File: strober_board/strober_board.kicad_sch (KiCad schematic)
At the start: 25 parts, among them J1 Conn_01x02, J2 Conn_01x02, J3 Conn_01x02, J4 AVR-ISP-6, Q1 BC237, Q2 BC237, Q3 BS170, SW1 SW_Push, U1 L78L05_TO92, U2 EL817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

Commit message: changed connectors
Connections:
- net at D3.2 (A), D4.1 (K): now also J3.1 (Pin_1); no longer J1.2 (Pin_2)
- net at D1.2 (A), D2.1 (K): now also J3.2 (Pin_2); no longer J1.1 (Pin_1)
- net at D6.1 (K), R5.2: now also J1.2 (Pin_2); no longer J3.1 (Pin_1)
- net at D6.2 (A), Q3.1 (D): now also J1.1 (Pin_1); no longer J3.2 (Pin_2)
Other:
- moved on the sheet: J1, J3
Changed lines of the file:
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@@
 	(symbol
 		(lib_id "Connector_Generic:Conn_01x02")
-		(at 97.79 82.55 0)
+		(at 30.48 59.69 180)
 		(unit 1)
 		(exclude_from_sim no)
@@
 		(dnp no)
 		(property "Reference" "J3"
-			(at 97.79 87.63 0)
+			(at 30.48 54.61 0)
 			(effects
 				(font
@@
 		)
 		(property "Value" "Conn_01x02"
-			(at 97.79 88.9 0)
+			(at 30.48 53.34 0)
 			(effects
 				(font
@@
 		)
 		(property "Footprint" "Connector_Molex:Molex_KK-254_AE-6410-02A_1x02_P2.54mm_Vertical"
-			(at 97.79 82.55 0)
+			(at 30.48 59.69 0)
 			(effects
 				(font
@@
 		)
 		(property "Datasheet" "~"
-			(at 97.79 82.55 0)
+			(at 30.48 59.69 0)
 			(effects
 				(font
@@
 		)
 		(property "Description" "Generic connector, single row, 01x02, script generated (kicad-library-utils/schlib/autogen/connector/)"
-			(at 97.79 82.55 0)
+			(at 30.48 59.69 0)
 			(effects
 				(font
@@
 	(symbol
 		(lib_id "Connector_Generic:Conn_01x02")
-		(at 30.48 57.15 0)
-		(mirror y)
+		(at 97.79 85.09 0)
+		(mirror x)
 		(unit 1)
 		(exclude_from_sim no)
@@
 		(dnp no)
 		(property "Reference" "J1"
-			(at 30.226 62.484 0)
+			(at 98.044 79.756 0)
 			(effects
 				(font
@@
 		)
 		(property "Value" "Conn_01x02"
-			(at 30.48 63.5 0)
+			(at 97.79 78.74 0)
 			(effects
 				(font
@@
 		)
 		(property "Footprint" "Connector_JST:JST_EH_B2B-EH-A_1x02_P2.50mm_Vertical"
-			(at 30.48 57.15 0)
+			(at 97.79 85.09 0)
 			(effects
 				(font
@@
 		)
 		(property "Datasheet" "~"
-			(at 30.48 57.15 0)
+			(at 97.79 85.09 0)
 			(effects
 				(font
@@
 		)
 		(property "Description" "Generic connector, single row, 01x02, script generated (kicad-library-utils/schlib/autogen/connector/)"
-			(at 30.48 57.15 0)
-			(effects
-				(font
+			(at 97.79 85.09 0)
+			(effects
+				(font

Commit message: firmware readme
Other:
- note added: "Fixme! Reverse polarity protection is flawed! Doesn't cover load path!"
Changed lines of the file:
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@@
+		)
+	)
+	(text "Fixme! Reverse polarity protection is flawed!\nDoesn't cover load path!"
+		(exclude_from_sim no)
+		(at 12.7 24.384 0)
+		(effects
+			(font
+				(size 1.27 1.27)
+				(thickness 0.254)
+				(bold yes)
+			)
+			(justify left)
 		)
 	)

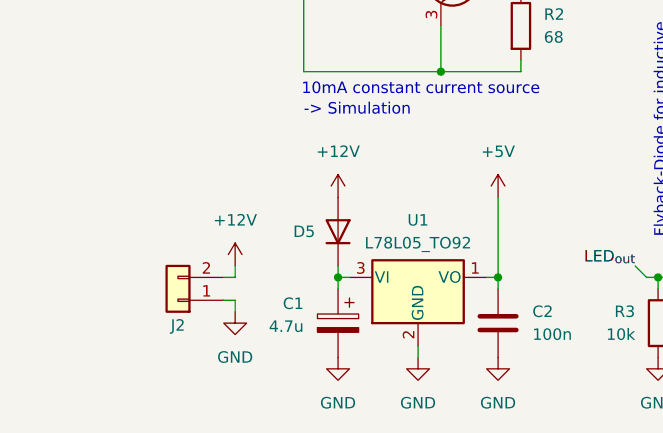
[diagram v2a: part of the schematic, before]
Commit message: Fixed reverse polarity protection
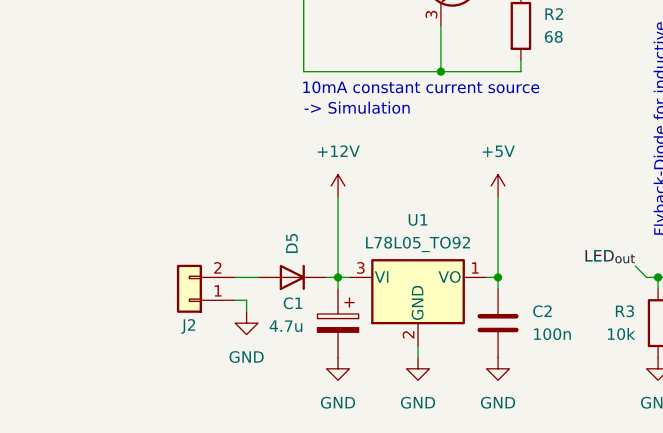
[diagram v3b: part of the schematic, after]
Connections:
- net +12V: now also C1.1, D5.1 (K), U1.3 (VI); no longer D5.2 (A), J2.2 (Pin_2)
- new net: D5.2 (A), J2.2 (Pin_2)
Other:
- moved on the sheet: D5, J2
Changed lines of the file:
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@@
 	(wire
 		(pts
-			(xy 35.56 95.25) (xy 36.83 95.25)
+			(xy 36.83 95.25) (xy 39.37 95.25)
 		)
 		(stroke
@@
 	(wire
 		(pts
-			(xy 36.83 97.79) (xy 35.56 97.79)
+			(xy 38.1 97.79) (xy 36.83 97.79)
 		)
 		(stroke
@@
 	(wire
 		(pts
-			(xy 36.83 99.06) (xy 36.83 97.79)
+			(xy 38.1 99.06) (xy 38.1 97.79)
 		)
 		(stroke
@@
 	(wire
 		(pts
-			(xy 48.26 93.98) (xy 48.26 95.25)
+			(xy 48.26 86.36) (xy 48.26 95.25)
 		)
 		(stroke
@@
 	(wire
 		(pts
-			(xy 36.83 95.25) (xy 36.83 93.98)
+			(xy 140.97 59.69) (xy 143.51 59.69)
 		)
 		(stroke
@@
 	(wire
 		(pts
-			(xy 140.97 59.69) (xy 143.51 59.69)
+			(xy 46.99 95.25) (xy 48.26 95.25)
 		)
 		(stroke
@@
 	(symbol
 		(lib_id "Device:D")
-		(at 48.26 90.17 270)
-		(mirror x)
+		(at 43.18 95.25 180)
 		(unit 1)
 		(exclude_from_sim no)
@@
 		(dnp no)
 		(property "Reference" "D5"
-			(at 45.72 90.17 90)
+			(at 43.18 92.71 90)
 			(effects
 				(font
@@
 		)
 		(property "Value" "D"
-			(at 45.72 91.4399 90)
+			(at 44.4499 92.71 90)
 			(effects
 				(font
@@
 		)
 		(property "Footprint" "Diode_THT:D_DO-15_P10.16mm_Horizontal"
-			(at 48.26 90.17 0)
+			(at 43.18 95.25 0)
 			(effects
 				(font
@@
 		)
 		(property "Datasheet" "~"
-			(at 48.26 90.17 0)
+			(at 43.18 95.25 0)
 			(effects
 				(font
@@
 		)
 		(property "Description" "Diode"
-			(at 48.26 90.17 0)
+			(at 43.18 95.25 0)
 			(effects
 				(font
@@
 		)
 		(property "Sim.Device" "D"
-			(at 48.26 90.17 0)
+			(at 43.18 95.25 0)
 			(effects
 				(font
@@
 		)
 		(property "Sim.Pins" "1=K 2=A"
-			(at 48.26 90.17 0)
+			(at 43.18 95.25 0)
 			(effects
 				(font
@@
 	(symbol
 		(lib_id "power:GND")
-		(at 36.83 99.06 0)
+		(at 38.1 99.06 0)
 		(unit 1)
 		(exclude_from_sim no)
@@
 		(fields_autoplaced yes)
 		(property "Reference" "#PWR02"
-			(at 36.83 105.41 0)
+			(at 38.1 105.41 0)
 			(effects
 				(font
@@
 		)
 		(property "Value" "GND"
-			(at 36.83 104.14 0)
+			(at 38.1 104.14 0)
 			(effects
 				(font
@@
 		)
 		(property "Footprint" ""
-			(at 36.83 99.06 0)
+			(at 38.1 99.06 0)
 			(effects
 				(font
@@
 		)
 		(property "Datasheet" ""
-			(at 36.83 99.06 0)
+			(at 38.1 99.06 0)
 			(effects
 				(font
@@
 		)
 		(property "Description" "Power symbol creates a global label with name \"GND\" , ground"
-			(at 36.83 99.06 0)
+			(at 38.1 99.06 0)
 			(effects
 				(font
@@
 	(symbol
 		(lib_id "Connector_Generic:Conn_01x02")
-		(at 30.48 97.79 180)
+		(at 31.75 97.79 180)
 		(unit 1)
 		(exclude_from_sim no)
@@
 		(dnp no)
 		(property "Reference" "J2"
-			(at 30.48 100.584 0)
+			(at 31.75 100.584 0)
 			(effects
 				(font
@@
 		)
 		(property "Value" "Conn_01x02"
-			(at 30.48 91.44 0)
+			(at 31.75 91.44 0)
 			(effects
 				(font
@@
 		)
 		(property "Footprint" "Connector_Molex:Molex_KK-254_AE-6410-02A_1x02_P2.54mm_Vertical"
-			(at 30.48 97.79 0)
+			(at 31.75 97.79 0)
 			(effects
 				(font
@@
 		)
 		(property "Datasheet" "~"
-			(at 30.48 97.79 0)
+			(at 31.75 97.79 0)
 			(effects
 				(font
@@
 		)
 		(property "Description" "Generic connector, single row, 01x02, script generated (kicad-library-utils/schlib/autogen/connector/)"
-			(at 30.48 97.79 0)
+			(at 31.75 97.79 0)
 			(effects
 				(font
@@
 					(unit 1)
 				)
-			)
-		)
-	)
-	(symbol
-		(lib_id "power:+12V")
-		(at 36.83 93.98 0)
-		(unit 1)
-		(exclude_from_sim no)
-		(in_bom yes)
-		(on_board yes)
-		(dnp no)
-		(fields_autoplaced yes)
-		(property "Reference" "#PWR01"
-			(at 36.83 97.79 0)
-			(effects
-				(font
-					(size 1.27 1.27)
-				)
-				(hide yes)
-			)
-		)
-		(property "Value" "+12V"
-			(at 36.83 88.9 0)
-			(effects
-				(font
-					(size 1.27 1.27)
-				)
-			)
-		)
-		(property "Footprint" ""
-			(at 36.83 93.98 0)
-			(effects
-				(font
-					(size 1.27 1.27)
-				)
-				(hide yes)
-			)
-		)
-		(property "Datasheet" ""
-			(at 36.83 93.98 0)
-			(effects
-				(font
-					(size 1.27 1.27)
-				)
-				(hide yes)
-			)
-		)
-		(property "Description" "Power symbol creates a global label with name \"+12V\""
-			(at 36.83 93.98 0)
-			(effects
-				(font
-					(size 1.27 1.27)
-				)
-				(hide yes)
-			)
-		)
-		(pin "1"
-		)
-		(instances
-			(project "whip_mod_board"
-				(path "/40cf83b7-ec3b-45bf-97f4-aa0389807d4b"
-					(reference "#PWR01")
-					(unit 1)
-				)

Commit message: minor board update
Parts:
- added C4: 100n, Resistor_THT:R_Axial_DIN0207_L6.3mm_D2.5mm_P10.16mm_Horizontal, symbol Device:C
- added J5: AVR-ISP-6, Connector_IDC:IDC-Header_2x03_P2.54mm_Vertical, symbol Connector:AVR-ISP-6
- added R6: 10k, Resistor_THT:R_Axial_DIN0207_L6.3mm_D2.5mm_P10.16mm_Horizontal, symbol Device:R
- added U4: ATtiny85-20P, Package_DIP:DIP-8_W7.62mm, symbol MCU_Microchip_ATtiny:ATtiny85-20P
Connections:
- net +5V: now also C4.1, J5.2 (VCC), R6.1, U4.8 (VCC)
- net GND: now also C4.2, J5.6 (GND), U4.4 (GND)
- net LED_{out}: now also U4.3 (XTAL2/PB4)
- net MISO: now also J5.1 (MISO), U4.6 (PB1)
- net MOSI: now also J5.4 (MOSI), U4.5 (AREF/PB0)
- net SCK: now also J5.3 (SCK), U4.7 (PB2)
- net Trigg_{in}: now also U4.2 (XTAL1/PB3)
- net ~{RST}: now also J5.5 (~{RST}), R6.2, U4.1 (~{RESET}/PB5)

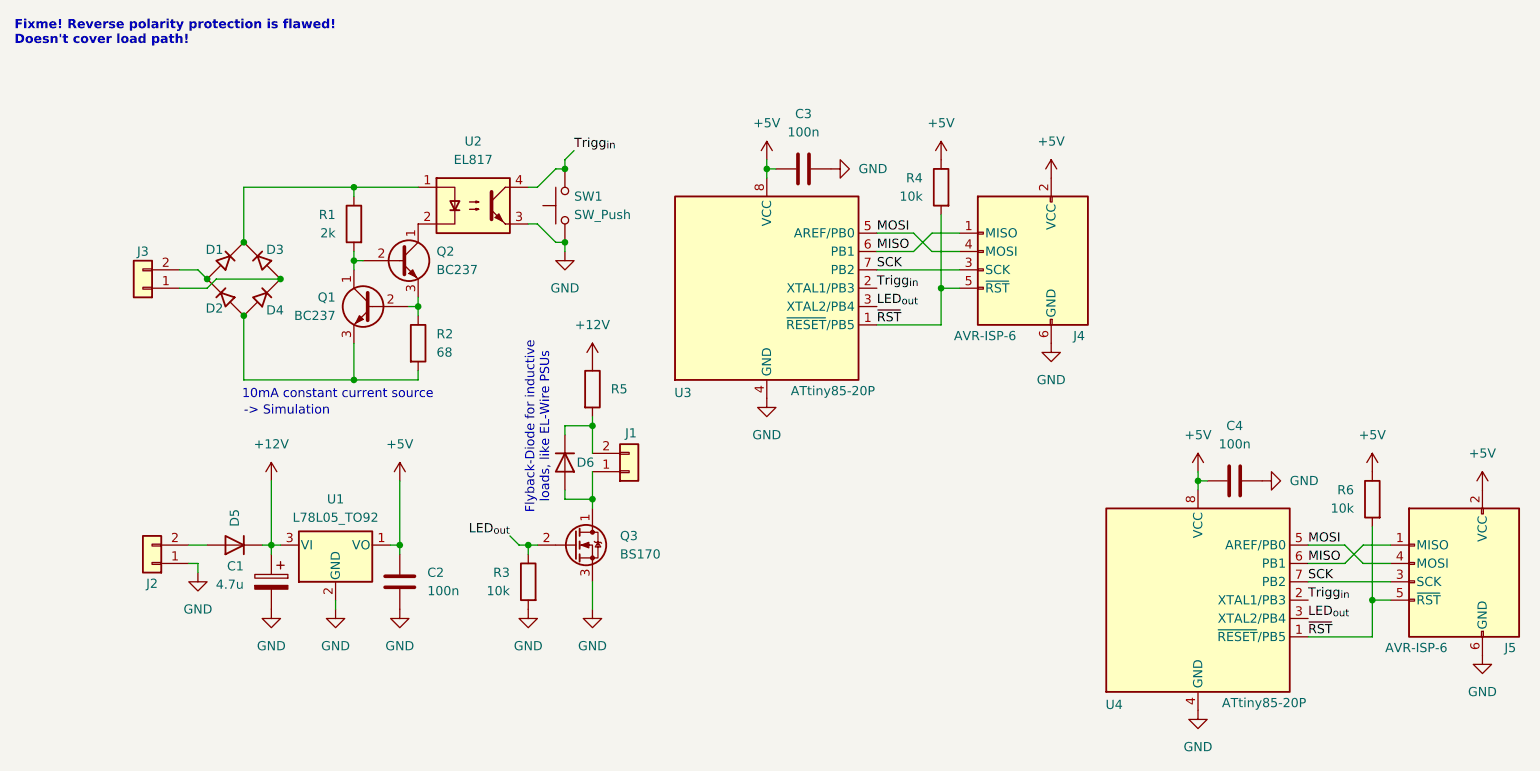
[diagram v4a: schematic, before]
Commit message: fix silkscreen typo
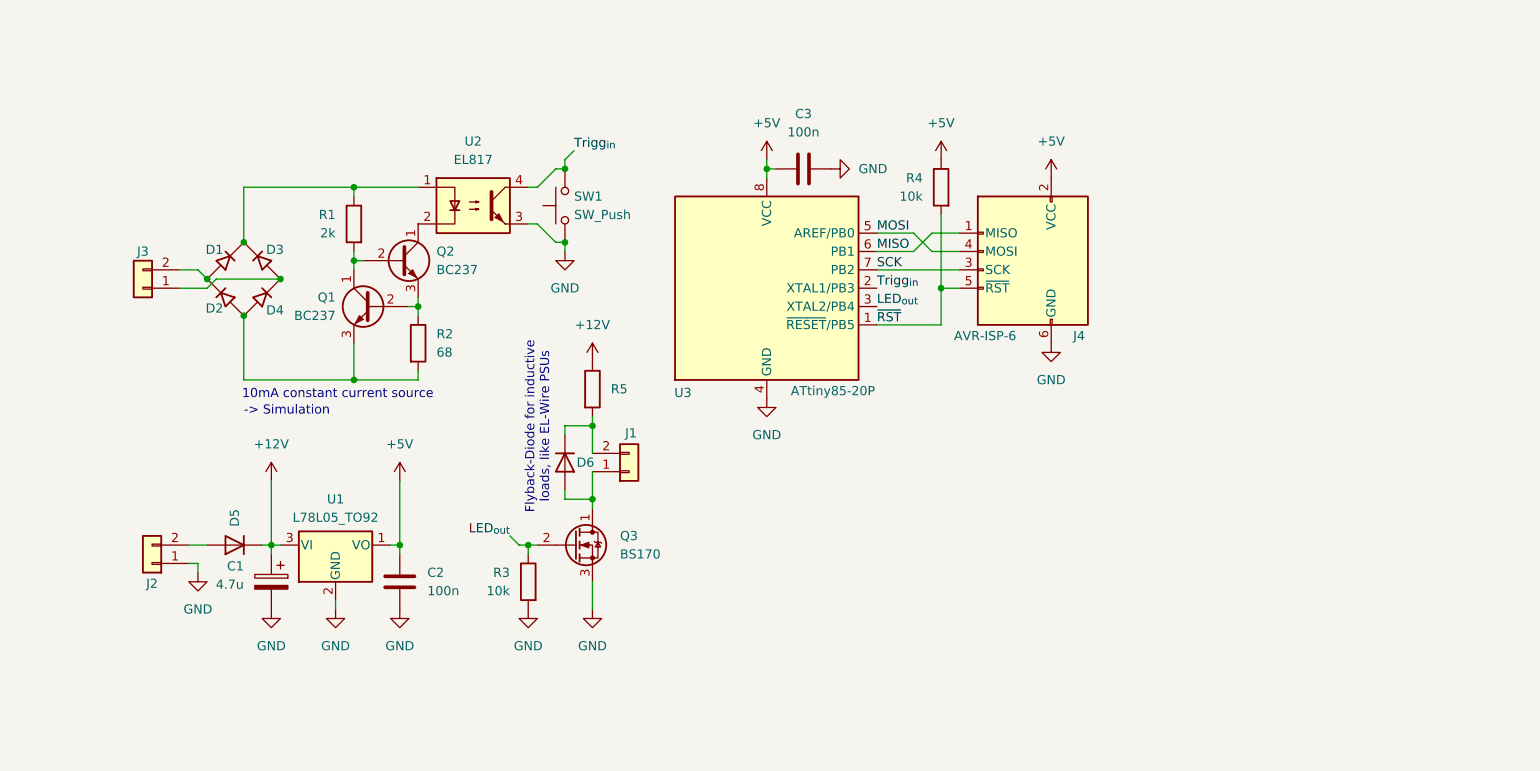
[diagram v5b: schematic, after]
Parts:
- removed C4: 100n, Resistor_THT:R_Axial_DIN0207_L6.3mm_D2.5mm_P10.16mm_Horizontal, symbol Device:C
- removed J5: AVR-ISP-6, Connector_IDC:IDC-Header_2x03_P2.54mm_Vertical, symbol Connector:AVR-ISP-6
- removed R6: 10k, Resistor_THT:R_Axial_DIN0207_L6.3mm_D2.5mm_P10.16mm_Horizontal, symbol Device:R
- removed U4: ATtiny85-20P, Package_DIP:DIP-8_W7.62mm, symbol MCU_Microchip_ATtiny:ATtiny85-20P
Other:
- note removed: "Fixme! Reverse polarity protection is flawed! Doesn't cover load path!"
